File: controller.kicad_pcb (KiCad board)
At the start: 2 copper layers, 50 x 25 mm, 0 parts

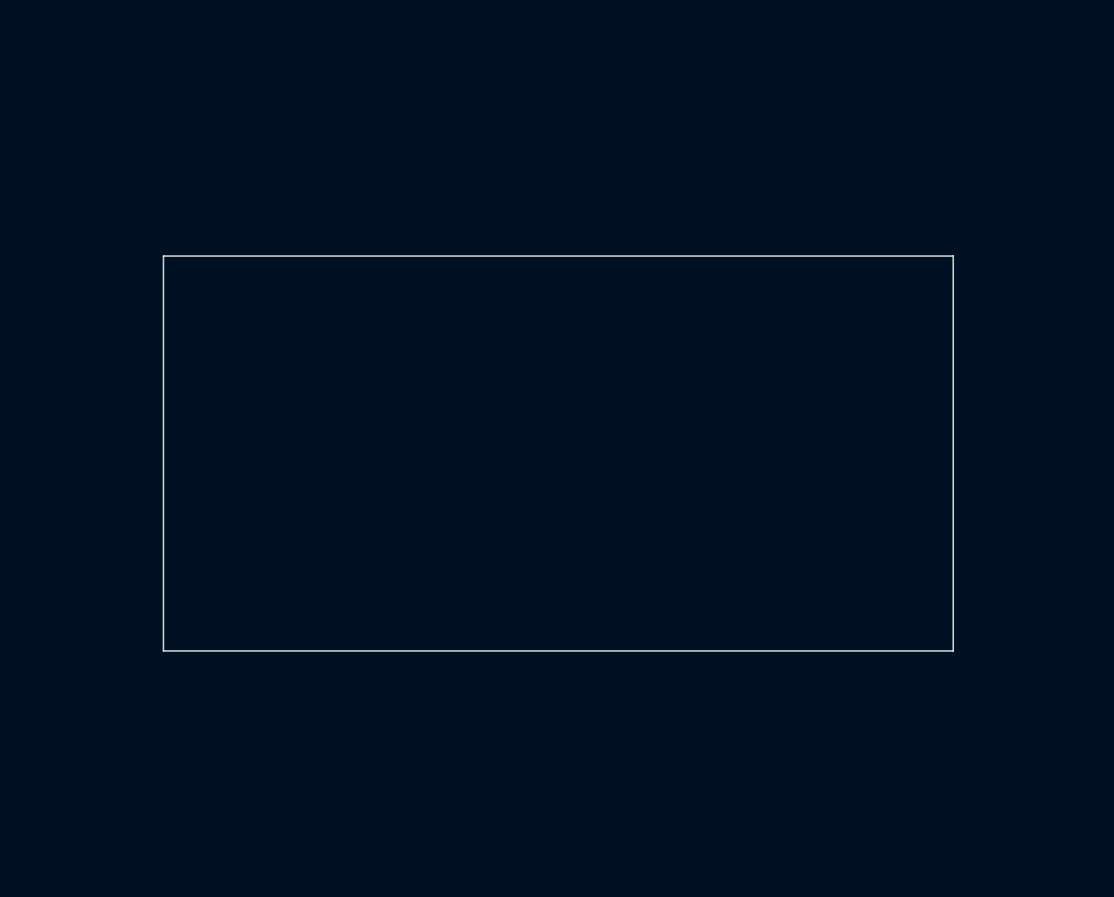
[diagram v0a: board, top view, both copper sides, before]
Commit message: Beautify silkscreen
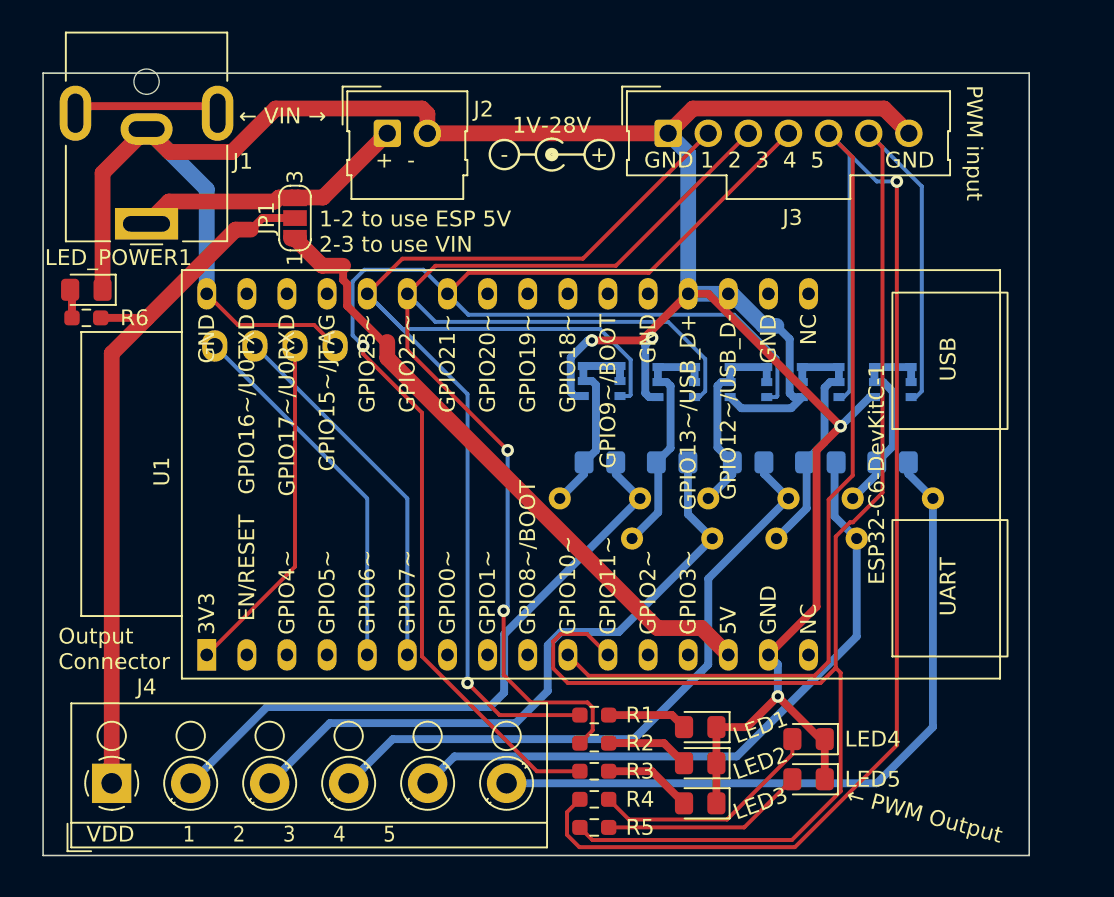
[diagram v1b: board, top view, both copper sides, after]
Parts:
- added Brd1: SSD1306, SSD1306:128x64OLED, B.Cu at (51.5, 54.5)
- added J1: Barrel_Jack_MountingPin, Connector_BarrelJack:BarrelJack_CUI_PJ-063AH_Horizontal, F.Cu at (43.2, 36.2)
- added J2: Conn_01x02_Pin, Connector_Molex:Molex_SL_171971-0002_1x02_P2.54mm_Vertical, F.Cu at (58.4, 30.5)
- added J3: Conn_01x07_Pin, Connector_Molex:Molex_SL_171971-0007_1x07_P2.54mm_Vertical, F.Cu at (76.2, 30.5)
- added J4: Screw_Terminal_01x06, TerminalBlock_RND:TerminalBlock_RND_205-00005_1x06_P5.00mm_Horizontal, F.Cu at (41.0, 71.6)
- added JP1: SolderJumper_3_Bridged12, Jumper:SolderJumper-3_P1.3mm_Open_RoundedPad1.0x1.5mm_NumberLabels, F.Cu at (52.6, 35.8)
- added LED1: LED, LED_SMD:LED_0805_2012Metric_Pad1.15x1.40mm_HandSolder, F.Cu at (78.2, 68.1)
- added LED2: LED, LED_SMD:LED_0805_2012Metric_Pad1.15x1.40mm_HandSolder, F.Cu at (78.2, 70.4)
- added LED3: LED, LED_SMD:LED_0805_2012Metric_Pad1.15x1.40mm_HandSolder, F.Cu at (78.2, 72.9)
- added LED4: LED, LED_SMD:LED_0805_2012Metric_Pad1.15x1.40mm_HandSolder, F.Cu at (85.1, 68.8)
- added LED5: LED, LED_SMD:LED_0805_2012Metric_Pad1.15x1.40mm_HandSolder, F.Cu at (85.1, 71.4)
- added LED_POWER1: LED, LED_SMD:LED_0805_2012Metric_Pad1.15x1.40mm_HandSolder, F.Cu at (39.4, 40.4)
- added Q1: IRLTS6342TRPBF, Package_SO:TSOP-6_1.65x3.05mm_P0.95mm, B.Cu at (72.0, 46.2)
- added Q2: IRLTS6342TRPBF, Package_SO:TSOP-6_1.65x3.05mm_P0.95mm, B.Cu at (76.7, 46.2)
- added Q3: IRLTS6342TRPBF, Package_SO:TSOP-6_1.65x3.05mm_P0.95mm, B.Cu at (81.3, 46.2)
- added Q4: IRLTS6342TRPBF, Package_SO:TSOP-6_1.65x3.05mm_P0.95mm, B.Cu at (85.9, 46.2)
- added Q5: IRLTS6342TRPBF, Package_SO:TSOP-6_1.65x3.05mm_P0.95mm, B.Cu at (90.4, 46.2)
- added R1: 15k, Resistor_SMD:R_0603_1608Metric_Pad0.98x0.95mm_HandSolder, F.Cu at (71.5, 67.3)
- added R2: 15k, Resistor_SMD:R_0603_1608Metric_Pad0.98x0.95mm_HandSolder, F.Cu at (71.5, 69.1)
- added R3: 15k, Resistor_SMD:R_0603_1608Metric_Pad0.98x0.95mm_HandSolder, F.Cu at (71.5, 70.9)
- added R4: 15k, Resistor_SMD:R_0603_1608Metric_Pad0.98x0.95mm_HandSolder, F.Cu at (71.5, 72.6)
- added R5: 15k, Resistor_SMD:R_0603_1608Metric_Pad0.98x0.95mm_HandSolder, F.Cu at (71.5, 74.4)
- added R6: 15k, Resistor_SMD:R_0603_1608Metric_Pad0.98x0.95mm_HandSolder, F.Cu at (39.4, 42.2)
- added REF**: Symbol_Barrel_Polarity, Symbol:Symbol_Barrel_Polarity, F.Cu at (68.8, 31.8)
- added REF**: KiCad-Logo2_8mm_SilkScreen, Symbol:KiCad-Logo2_8mm_SilkScreen, B.Cu at (94.0, 65.1)
- added REF**: OSHW-Logo_11.4x12mm_SilkScreen, Symbol:OSHW-Logo_11.4x12mm_SilkScreen, B.Cu at (81.5, 70.4)
- added RoutSMD1: 0, Resistor_SMD:R_0805_2012Metric_Pad1.20x1.40mm_HandSolder, B.Cu at (71.9, 51.3)
- added RoutSMD2: 0, Resistor_SMD:R_0805_2012Metric_Pad1.20x1.40mm_HandSolder, B.Cu at (76.5, 51.3)
- added RoutSMD3: 0, Resistor_SMD:R_0805_2012Metric_Pad1.20x1.40mm_HandSolder, B.Cu at (81.3, 51.3)
- added RoutSMD4: 0, Resistor_SMD:R_0805_2012Metric_Pad1.20x1.40mm_HandSolder, B.Cu at (85.8, 51.3)
- added RoutSMD5: 0, Resistor_SMD:R_0805_2012Metric_Pad1.20x1.40mm_HandSolder, B.Cu at (90.4, 51.3)
- added RoutTH1: 0, Resistor_THT:R_Axial_DIN0204_L3.6mm_D1.6mm_P5.08mm_Horizontal, B.Cu at (74.4, 53.6)
- added RoutTH2: 0, Resistor_THT:R_Axial_DIN0204_L3.6mm_D1.6mm_P5.08mm_Horizontal, B.Cu at (79.0, 56.1)
- added RoutTH3: 0, Resistor_THT:R_Axial_DIN0204_L3.6mm_D1.6mm_P5.08mm_Horizontal, B.Cu at (83.8, 53.6)
- added RoutTH4: 0, Resistor_THT:R_Axial_DIN0204_L3.6mm_D1.6mm_P5.08mm_Horizontal, B.Cu at (88.1, 56.1)
- added RoutTH5: 0, Resistor_THT:R_Axial_DIN0204_L3.6mm_D1.6mm_P5.08mm_Horizontal, B.Cu at (93.0, 53.6)
- added U1: ESP32-C6-DevKitC-1, Espressif:ESP32-C6-DevKitC-1, F.Cu at (47.0, 63.5)
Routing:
- net GND: track 0.00 -> 185.2 mm, vias 0 -> 4
- net /PWM4: track 0.00 -> 137.6 mm, vias 0 -> 1
- net /PWM5: track 0.00 -> 104.7 mm
- net /PWM3: track 0.00 -> 97.0 mm, vias 0 -> 1
- net /PWM2: track 0.00 -> 85.2 mm, vias 0 -> 2
- net /PWM1: track 0.00 -> 82.4 mm, vias 0 -> 1
- net /OUT5: track 0.00 -> 45.9 mm
- net VDD: track 0.00 -> 45.3 mm
- net /OUT4: track 0.00 -> 42.5 mm
- net /OUT2: track 0.00 -> 41.6 mm
- net /OUT3: track 0.00 -> 41.4 mm
- net /OUT1: track 0.00 -> 41.0 mm
- net +5V: track 0.00 -> 40.3 mm
- net /I2C_SDA: track 0.00 -> 23.6 mm
- net /I2C_SCL: track 0.00 -> 23.6 mm
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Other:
- board size 50 x 25 mm -> 62.4 x 49.5 mm
- board text added: "+"
- board text added: "+ -"
- board text added: "-"
- board text added: "1 2 3 4 5"
- board text added: "1-2 to use ESP 5V 2-3 to use VIN"
- board text added: "1V-28V"
- board text added: "3V3"
- board text added: "GND"
- board text added: "Optional SSD1306 screen"
- board text added: "Output Connector"
- board text added: "PWM input"
- board text added: "SCL"
- board text added: "SDA"
- board text added: "Short-circuit Rout, or add desired series resistance"
- board text added: "VDD"
- board text added: "← PWM Output"
- board text added: "← VIN →"

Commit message: Add button
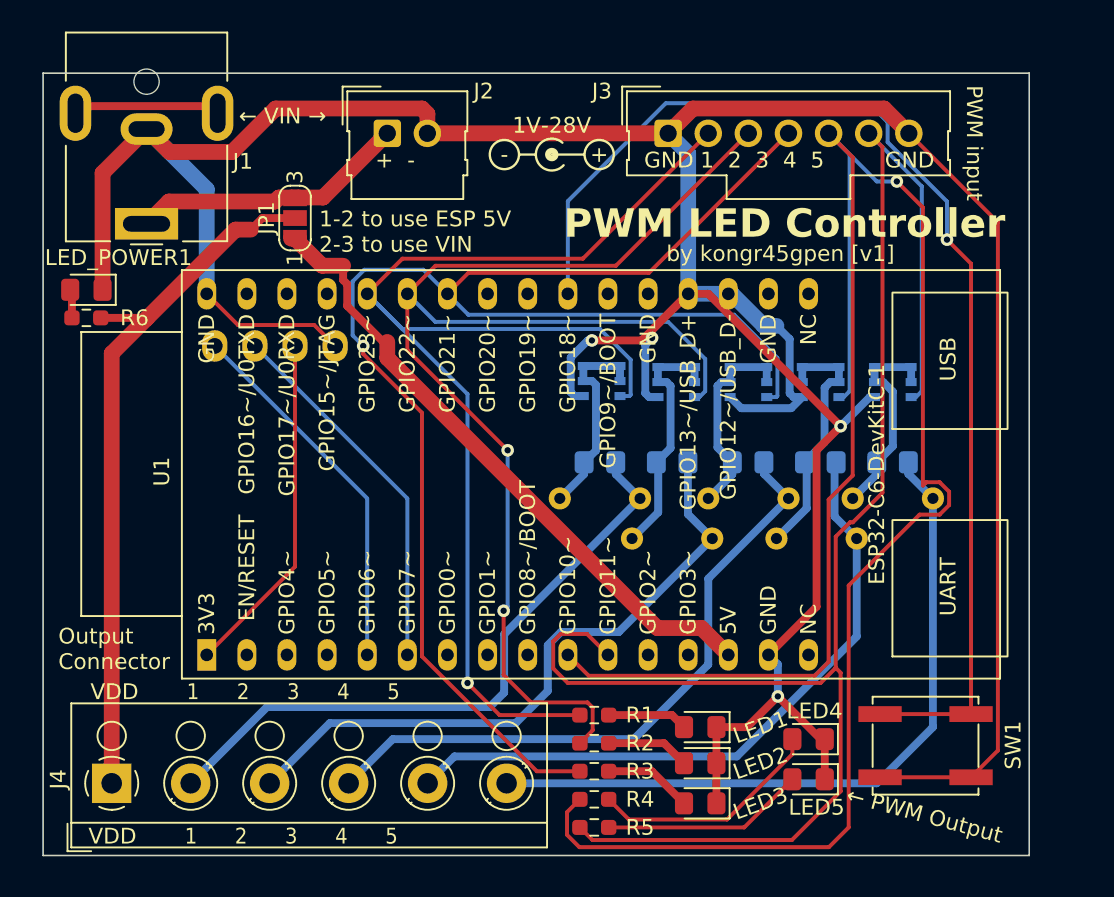
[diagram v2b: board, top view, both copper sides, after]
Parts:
- added SW1: SW_Push, Button_Switch_SMD:SW_SPST_EVQP0, F.Cu at (92.5, 69.2)
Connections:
- U1 pad 23: unconnected-(U1-GPIO18-Pad23) -> Net-(U1-GPIO18)
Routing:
- net Net-(U1-GPIO18): track 0.00 -> 74.6 mm, vias 0 -> 1
- net GND: track 185.2 -> 234.8 mm
- net /PWM4: track 137.6 -> 143.3 mm
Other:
- board text added: "PWM LED Controller"
- board text added: "by kongr45gpen [v1]"
- board text added: "https://github.com/kongr45gpen/led-controller-pcb.git"

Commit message: Add figures
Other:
- board size 62.4 x 49.5 mm -> 62.5 x 49.5 mm
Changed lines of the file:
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@@
   )
   (gr_rect (start 36.63 26.67) (end 99.06 76.2)
-    (stroke (width 0.1) (type default)) (fill none) (layer "Edge.Cuts"))
+    (stroke (width 0.1) (type default)) (fill none) (layer "Cmts.User"))
+  (gr_line (start 36.6 76.1) (end 36.6 26.6)
+    (stroke (width 0.1) (type default)) (layer "Edge.Cuts"))
+  (gr_line (start 99.1 76.1) (end 36.6 76.1)
+    (stroke (width 0.1) (type default)) (layer "Edge.Cuts"))
+  (gr_line (start 99.1 26.6) (end 99.1 76.1)
+    (stroke (width 0.1) (type default)) (layer "Edge.Cuts"))
+  (gr_line (start 36.6 26.6) (end 99.1 26.6)
+    (stroke (width 0.1) (type default)) (layer "Edge.Cuts"))
   (gr_text "3V3" (at 52.578 45.72 270) (layer "B.SilkS")
     (effects (font (size 1 1) (thickness 0.15)) (justify right mirror))

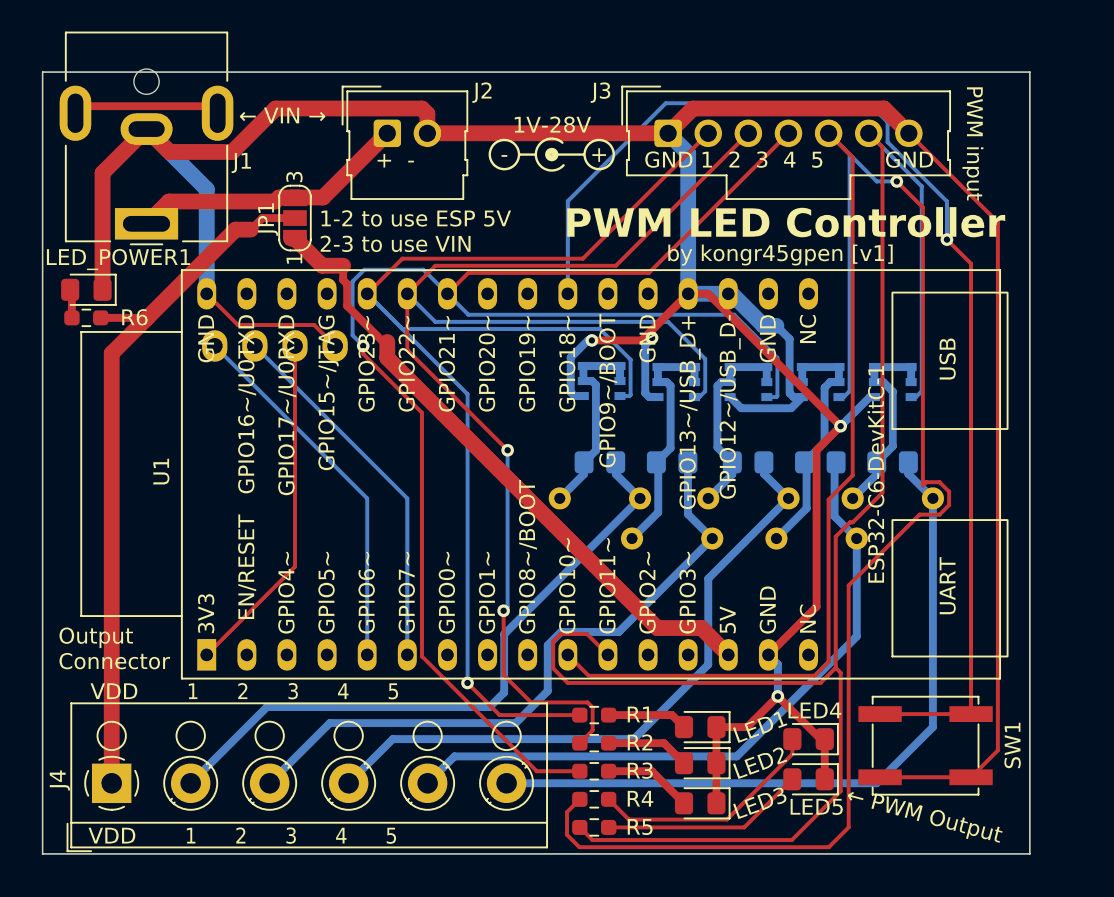
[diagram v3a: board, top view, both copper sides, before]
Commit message: Increase board height to fit barrel jack pin
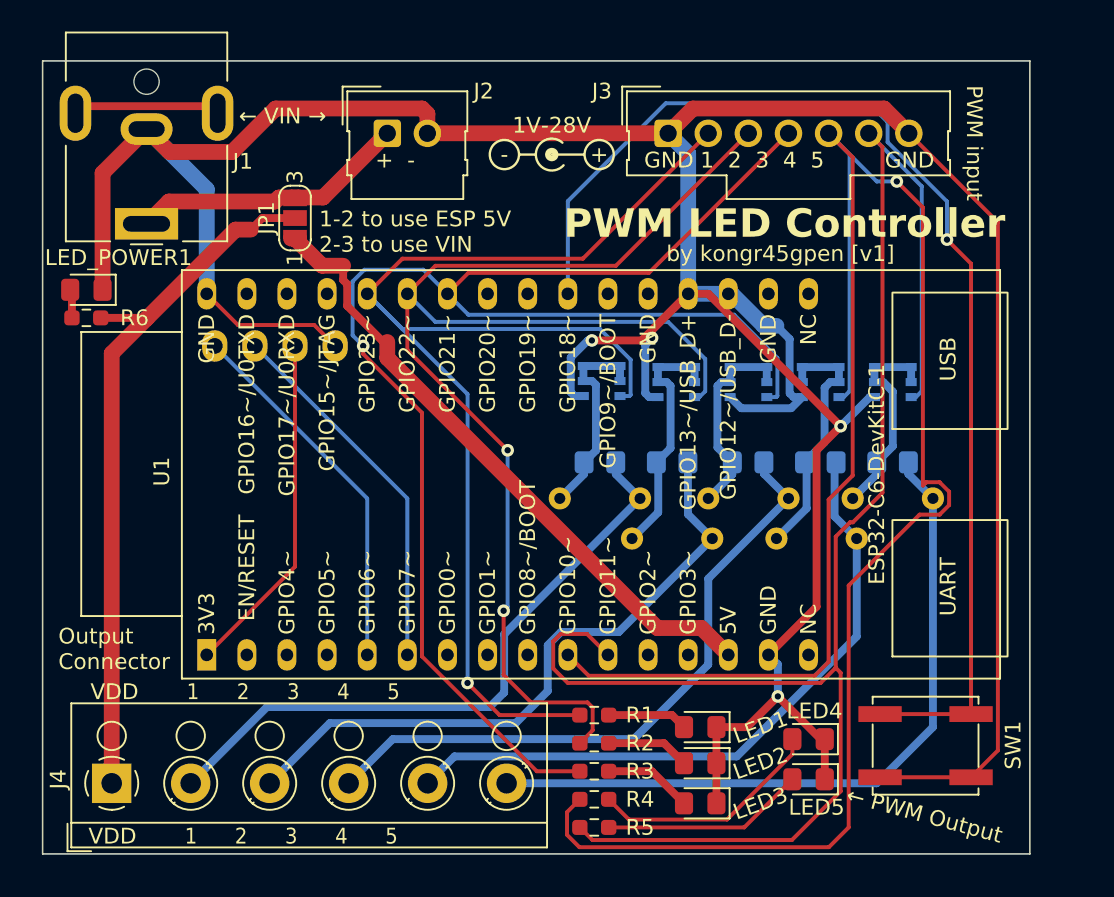
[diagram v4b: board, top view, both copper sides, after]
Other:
- board size 62.5 x 49.5 mm -> 62.5 x 50.2 mm
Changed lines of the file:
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@@
     )
   )
-  (gr_rect (start 36.63 26.67) (end 99.06 76.2)
+  (gr_rect (start 36.63 25.77) (end 99.06 76.2)
     (stroke (width 0.1) (type default)) (fill none) (layer "Cmts.User"))
-  (gr_line (start 36.6 76.1) (end 36.6 26.6)
+  (gr_line (start 36.6 76.1) (end 36.6 25.9)
     (stroke (width 0.1) (type default)) (layer "Edge.Cuts"))
   (gr_line (start 99.1 76.1) (end 36.6 76.1)
     (stroke (width 0.1) (type default)) (layer "Edge.Cuts"))
-  (gr_line (start 99.1 26.6) (end 99.1 76.1)
+  (gr_line (start 99.1 25.9) (end 99.1 76.1)
     (stroke (width 0.1) (type default)) (layer "Edge.Cuts"))
-  (gr_line (start 36.6 26.6) (end 99.1 26.6)
+  (gr_line (start 36.6 25.9) (end 99.1 25.9)
     (stroke (width 0.1) (type default)) (layer "Edge.Cuts"))
   (gr_text "3V3" (at 52.578 45.72 270) (layer "B.SilkS")

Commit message: Updates for PCB v2
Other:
- board text added: "by kongr45gpen [v2]"
- board text removed: "by kongr45gpen [v1]"
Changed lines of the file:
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@@
     (effects (font (size 1.8 1.8) (thickness 0.35) bold))
   )
-  (gr_text "by kongr45gpen [v1]" (at 83.312 38.1) (layer "F.SilkS")
+  (gr_text "by kongr45gpen [v2]" (at 83.312 38.1) (layer "F.SilkS")
     (effects (font (size 1 1) (thickness 0.15)))
   )

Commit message: Complete routing
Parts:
- removed the REF** at (94.0, 65.1)
- removed the REF** at (81.5, 70.4)
- removed RoutSMD1, RoutSMD2, RoutSMD3, RoutSMD4, RoutSMD5: 0, Resistor_SMD:R_0805_2012Metric_Pad1.20x1.40mm_HandSolder
- removed RoutTH1, RoutTH2, RoutTH3, RoutTH4, RoutTH5: 0, Resistor_THT:R_Axial_DIN0204_L3.6mm_D1.6mm_P5.08mm_Horizontal
- added C1: 100n, Capacitor_SMD:C_0603_1608Metric_Pad1.08x0.95mm_HandSolder, F.Cu at (60.5, 30.5)
- added J5: Conn_01x03_Pin, Connector_Molex:Molex_SL_171971-0003_1x03_P2.54mm_Vertical, F.Cu at (66.5, 30.0)
- added JP2: SolderJumper_3_Bridged12, Jumper:SolderJumper-3_P1.3mm_Open_RoundedPad1.0x1.5mm_NumberLabels, F.Cu at (68.9, 36.6)
- added JP3: SolderJumper_2_Bridged, Jumper:SolderJumper-2_P1.3mm_Bridged_RoundedPad1.0x1.5mm, B.Cu at (43.4, 48.5)
- added JP4: SolderJumper_2_Open, Jumper:SolderJumper-2_P1.3mm_Open_RoundedPad1.0x1.5mm, B.Cu at (82.5, 69.3)
- added JPout1: SolderJumper_2_Open, Jumper:SolderJumper-2_P1.3mm_Open_TrianglePad1.0x1.5mm, B.Cu at (71.9, 53.6)
- added JPout2: SolderJumper_2_Open, Jumper:SolderJumper-2_P1.3mm_Open_TrianglePad1.0x1.5mm, B.Cu at (76.7, 53.6)
- added JPout3: SolderJumper_2_Open, Jumper:SolderJumper-2_P1.3mm_Open_TrianglePad1.0x1.5mm, B.Cu at (81.0, 53.6)
- added JPout4: SolderJumper_2_Open, Jumper:SolderJumper-2_P1.3mm_Open_TrianglePad1.0x1.5mm, B.Cu at (85.9, 53.6)
- added JPout5: SolderJumper_2_Open, Jumper:SolderJumper-2_P1.3mm_Open_TrianglePad1.0x1.5mm, B.Cu at (90.6, 53.6)
- added REF**: KiCad-Logo2_5mm_SilkScreen, Symbol:KiCad-Logo2_5mm_SilkScreen, B.Cu at (95.5, 46.7)
- added REF**: OSHW-Logo_7.5x8mm_SilkScreen, Symbol:OSHW-Logo_7.5x8mm_SilkScreen, B.Cu at (74.4, 70.6)
- added Rpd1: 100k, Resistor_SMD:R_0603_1608Metric_Pad0.98x0.95mm_HandSolder, B.Cu at (71.9, 45.7)
- added Rpd2: 100k, Resistor_SMD:R_0603_1608Metric_Pad0.98x0.95mm_HandSolder, B.Cu at (76.7, 45.7)
- added Rpd3: 100k, Resistor_SMD:R_0603_1608Metric_Pad0.98x0.95mm_HandSolder, B.Cu at (81.3, 45.7)
- added Rpd4: 100k, Resistor_SMD:R_0603_1608Metric_Pad0.98x0.95mm_HandSolder, B.Cu at (85.9, 45.7)
- added Rpd5: 100k, Resistor_SMD:R_0603_1608Metric_Pad0.98x0.95mm_HandSolder, B.Cu at (90.4, 45.7)
- added VR1: Wurth Elektronik 1769405x41, controller_library:1769405x41, B.Cu at (91.9, 64.0)
- J1: footprint Connector_BarrelJack:BarrelJack_CUI_PJ-063AH_Horizontal -> Connector_BarrelJack:BarrelJack_CUI_PJ-063AH_Horizontal_CircularHoles
- SW1: footprint Button_Switch_SMD:SW_SPST_EVQP0 -> controller_library:SWITCH-4
- moved REF** 18.9 mm to (49.9, 30.9), turned to 90 degrees
- moved J2 4.35 mm to (54.1, 30.0)
- moved J3 2.81 mm to (79.0, 30.2)
- moved Q1 2.62 mm to (72.0, 48.8)
- moved Q2 2.62 mm to (76.7, 48.8)
- moved Q3 2.62 mm to (81.3, 48.8)
- moved Q4 2.62 mm to (85.9, 48.8)
- moved Q5 2.62 mm to (90.4, 48.8)
- moved JP1 0.73 mm to (52.6, 36.6), turned to 180 degrees
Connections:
- net Net-(J2-Pin_1) renamed /VIN
- J1 pad 2: GND -> GNDPWR
- J2 pad 2: GND -> GNDPWR
- LED_POWER1 pad 1: GND -> GNDPWR
- Q1 pad 4: GND -> GNDPWR
- Q2 pad 4: GND -> GNDPWR
- Q3 pad 4: GND -> GNDPWR
- Q4 pad 4: GND -> GNDPWR
- Q5 pad 4: GND -> GNDPWR
- U1 pad 25: unconnected-(U1-GPIO20-Pad25) -> /ADDR_LED_OUT
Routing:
- net GND: track 234.8 -> 85.7 mm, vias 4 -> 7
- net /VIN: track 17.6 -> 104.8 mm
- net /PWM4: track 143.3 -> 75.2 mm, vias 1 -> 2
- net Net-(U1-GPIO18): track 74.6 -> 41.1 mm, vias 1 -> 0
- net GNDPWR: track 0.00 -> 27.0 mm, vias 0 -> 7
- net +5V: track 40.3 -> 56.1 mm
- net /PWM3: track 97.0 -> 81.2 mm
- net /PWM5: track 104.7 -> 90.6 mm, vias 0 -> 2
- net /ADDR_LED_OUT: track 0.00 -> 12.5 mm, vias 0 -> 1
- net /PWM1: track 82.4 -> 72.9 mm, vias 1 -> 2
- net /OUT4: track 42.5 -> 34.7 mm
- net Net-(J5-Pin_3): track 0.00 -> 7.75 mm
- net /OUT3: track 41.4 -> 34.7 mm
- net /OUT5: track 45.9 -> 40.0 mm
- net Net-(JPout4-B): track 16.0 -> 10.2 mm
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- added copper zone on F.Cu, net GND
- added copper zone on B.Cu, net GNDPWR
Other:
- board text added: "(GND)"
- board text added: "1-28V"
- board text added: "1-2: U5V 2-3: VIN"
- board text added: "5V"
- board text added: "D"
- board text added: "PWM in/out"
- board text added: "REG from VIN to 5V"
- board text added: "Short to enable VR"
- board text added: "Short-circuit JPout, or add desired series resistance"
- board text added: "↑ Addr ↑"
- board text added: "↑ VIN ↑"
- board text added: "↓ Addr ↓"
- board text removed: "1-2 to use ESP 5V 2-3 to use VIN"
- board text removed: "1V-28V"
- board text removed: "PWM input"
- board text removed: "Short-circuit Rout, or add desired series resistance"
- board text removed: "← VIN →"
